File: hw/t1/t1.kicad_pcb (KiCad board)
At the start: 4 copper layers, 63.5 x 11.8 mm, 65 parts, among them J1 SFP edge (INF-8074i), J2 Rosenberger E6S20A-40MT5-Z (H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, U1 DP83TG720S-Q1 (or DP83TC812S-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, U2 STM32G031F6P6, U3 TPS62822DLC, U4 TPS22918DBVR, Y1 25MHz CL8pF 2016

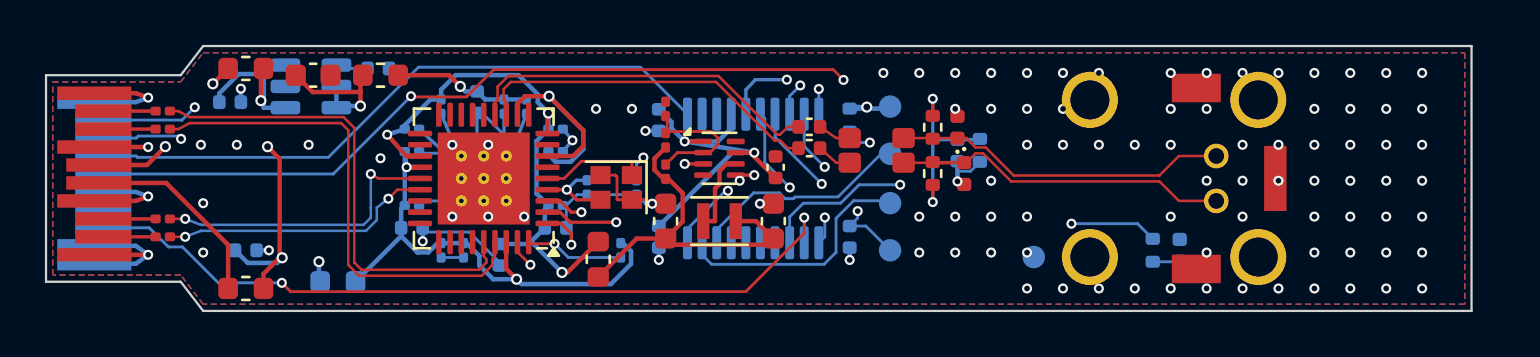
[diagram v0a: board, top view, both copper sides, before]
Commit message: SFP edge was mirrored: fix the pad order, re-lay T1
The edge footprint put pin 20 at the top seen from above with the card edge
on the left; SFF-8419 Figure 7-2 (and INF-8074i Figure 2, drawn the other
way round) has pin 11 there. Every host contact would have landed between
two pads, VccT against ground. pad_y() is negated, the ground-finger vias
follow, and tools/compliance.py now states the expected positions itself.

T1, re-laid on the corrected edge:
- TD reaches the PHY's TX pins and RD its RX pins straight, P to P, both on
  top; the SGMII polarity-invert bits the firmware used to set are gone
- DP83TG720 EP 3.7 mm (RHA0036A), not 4.1
- XI series resistor R9: 0 ohm for the DP83TG720, 100 ohm in the DP83TC812
  loadout (SNLS654D Table 5-1)
- firmware clears SGMII AN on the DP83TC812 (SNLS654D 7.4.12.4)

Shared footprints: CMC land to TDK ACT1210E / Murata DLW32MH (1.05 x 0.6
pads, 0.4 between lines, 2.0 inner gap), H-MTD front solder area 2.2 wide
(MB_633), board thickness 1.0 mm in the files.

RJ45 and T1S still carry the mirrored edge; the README says not to order.
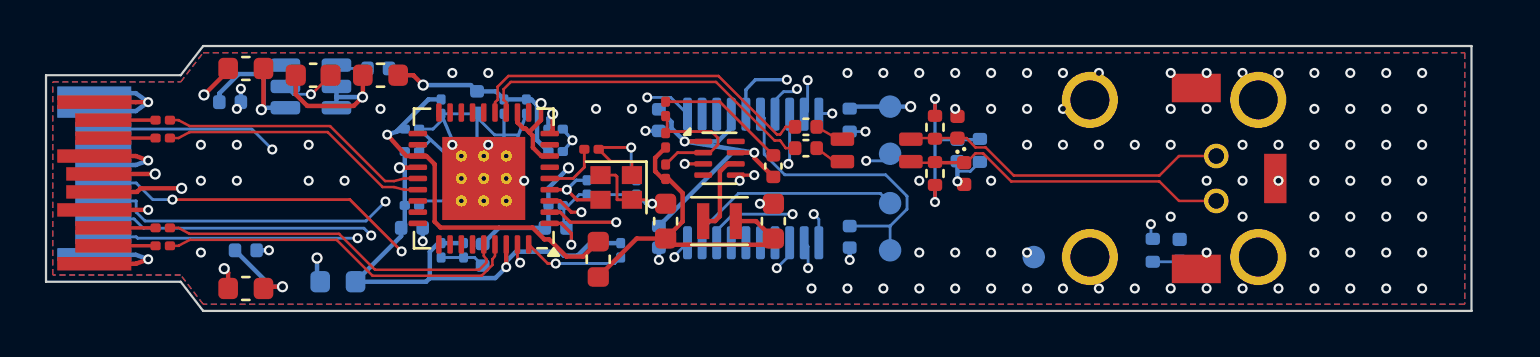
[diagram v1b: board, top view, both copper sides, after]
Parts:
- added R9: 0, Resistor_SMD:R_0201_0603Metric, F.Cu at (124.3, 98.7)
- U1: footprint Package_DFN_QFN:QFN-36-1EP_6x6mm_P0.5mm_EP4.1x4.1mm_ThermalVias -> Package_DFN_QFN:QFN-36-1EP_6x6mm_P0.5mm_EP3.7x3.7mm_ThermalVias
- moved FB1 9.80 mm to (108.9, 104.9)
- moved FB2 9.80 mm to (108.9, 95.1)
- moved C4 6.00 mm to (105.2, 103.0)
- moved C6 5.20 mm to (105.2, 97.4)
- moved C3 4.40 mm to (105.2, 102.2)
- moved C5 3.60 mm to (105.2, 98.2)
- moved C21 0.75 mm to (119.5, 103.4)
- moved C33 0.15 mm to (133.8, 97.7)
- moved C34 0.15 mm to (133.8, 98.7)
- moved C26 0.11 mm to (132.4, 99.5)
- moved R6 0.10 mm to (139.6, 97.7)
- moved R7 0.10 mm to (139.6, 99.8)
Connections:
- C24 pad 1: XI -> XI_X
- C3 pad 2: SG_TX_N -> SG_TX_P
- C4 pad 2: SG_TX_P -> SG_TX_N
- C5 pad 2: SG_RX_N -> SG_RX_P
- C6 pad 2: SG_RX_P -> SG_RX_N
- Y1 pad 1: XI -> XI_X
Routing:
- net SCL: track 48.8 -> 28.3 mm
- net TX_FAULT: track 47.0 -> 32.6 mm
- net VDD1P0: track 24.4 -> 36.0 mm
- net VDDA: track 22.0 -> 13.5 mm
- net GND: track 60.3 -> 67.2 mm, vias 106 -> 115
- net SG_TX_P: track 21.6 -> 15.9 mm
- net SG_TX_N: track 22.0 -> 16.3 mm
- net XI_X: track 0.00 -> 5.36 mm, vias 0 -> 1
- net TX_DISABLE: track 45.8 -> 49.7 mm
- net XI: track 6.41 -> 2.55 mm, vias 1 -> 0
- net SDA: track 28.6 -> 31.8 mm, vias 0 -> 2
- net RX_LOS: track 35.3 -> 38.1 mm
- net NRST: track 15.7 -> 13.5 mm, vias 2 -> 0
- net +3V3: track 61.3 -> 59.4 mm
- net MDC: track 18.0 -> 16.5 mm
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
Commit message: T1: TI's OPEN Alliance MDI termination; bring-up order; honest README
- R6/R7 are now 1 k 1 % 0.75 W 2010 (RC2010FK-071KL), SNLA371B's
  configuration, along the board either side of the pair; the H-MTD and the
  board end moved 1 mm back (64.5 mm) to make the room. The unfitted 0402
  ESD footprints, not in TI's configuration, are gone.
- The DC block stays 100 nF 100 V X5R +-10 %: JLC stocks no SMD 1 % part
  at 100 V, nor a 0402 X7R (REFERENCES.md says so).
- Bottom-row escapes for VDDIO and LED0, a ground via for the decap pocket
  under U1, the TX pair 0.1 mm lower to let it in. DRC 0 / 0 unconnected,
  ERC 0, KiCad 9 PASS, panel 0 errors.
- ORDER.md: check pin 11/20 on the Gerbers; bring-up on a current-limited
  bench supply, then I2C 0x50/0x51/0x56, then one known host.
- README: what is SFP-standard and what is not (no SFF-8024 code for
  BASE-T1 / T1S; the EEPROM personality is a workaround), host SGMII and
  2500BASE-X requirements; RJ45/T1S marked do-not-order.
- COMPLIANCE.md regenerated: the independent edge check now fails RJ45/T1S.
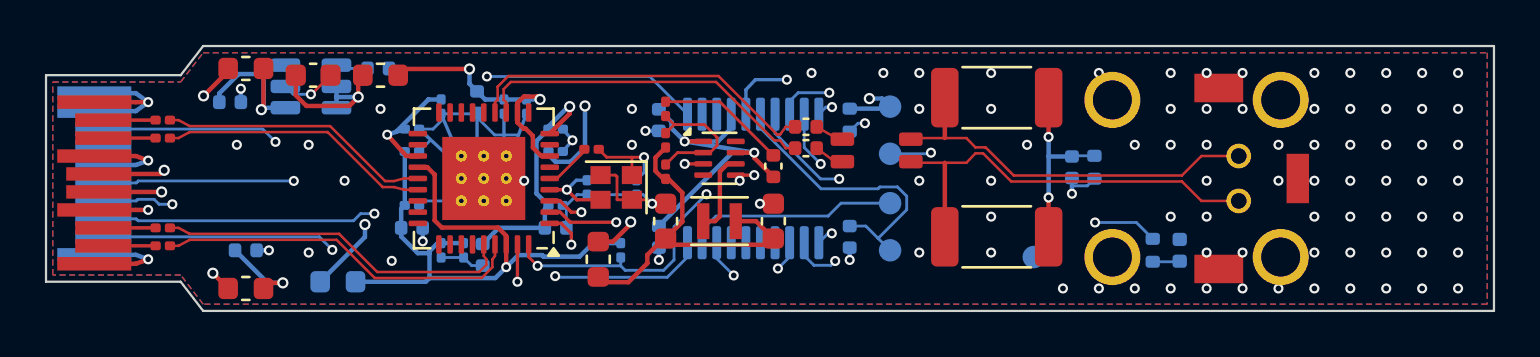
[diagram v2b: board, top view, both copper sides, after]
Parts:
- removed D2, D3: ESD (DNP), Diode_SMD:D_0402_1005Metric
- R6, R7: value 1k 1% 0.2W -> 1k 1% 0.75W; footprint Resistor_SMD:R_0402_1005Metric -> Resistor_SMD:R_2010_5025Metric
- moved C35 5.15 mm to (145.7, 99.5)
- moved R8 5.15 mm to (146.7, 99.5)
- moved R7 3.94 mm to (142.3, 102.6), turned to 0 degrees
- moved R6 3.05 mm to (142.3, 96.4), turned to 0 degrees
- moved J2 1.00 mm to (155.0, 100.0)
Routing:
- net TX_DISABLE: track 49.7 -> 40.6 mm
- net SWDIO: track 9.68 -> 16.2 mm
- net MDC: track 16.5 -> 22.1 mm
- net VDDA: track 13.5 -> 18.1 mm, vias 2 -> 3
- net MDI_N: track 16.4 -> 20.5 mm
- net VDDIO: track 24.5 -> 28.7 mm, vias 2 -> 1
- net MDIO: track 19.0 -> 22.6 mm, vias 2 -> 3
- net MDI_P: track 15.1 -> 18.3 mm
- net VDD1P0: track 36.0 -> 33.0 mm
- net +3V3: track 59.4 -> 61.5 mm
- net SDA: track 31.8 -> 29.7 mm
- net XI_X: track 5.36 -> 4.13 mm
- net SCL: track 28.3 -> 29.4 mm, vias 3 -> 2
- net MDI_CT: track 8.22 -> 9.10 mm
- net LED0: track 31.0 -> 31.8 mm
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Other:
- board size 63.5 x 11.8 mm -> 64.5 x 11.8 mm
